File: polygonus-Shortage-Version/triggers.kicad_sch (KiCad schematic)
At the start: 29 parts, among them U10 SRV05-4, U1202 SN74LVC2G17DB, U1207 SN74LVC2G17DB, U1208 SN74LVC2G17DB, U7 SRV05-4

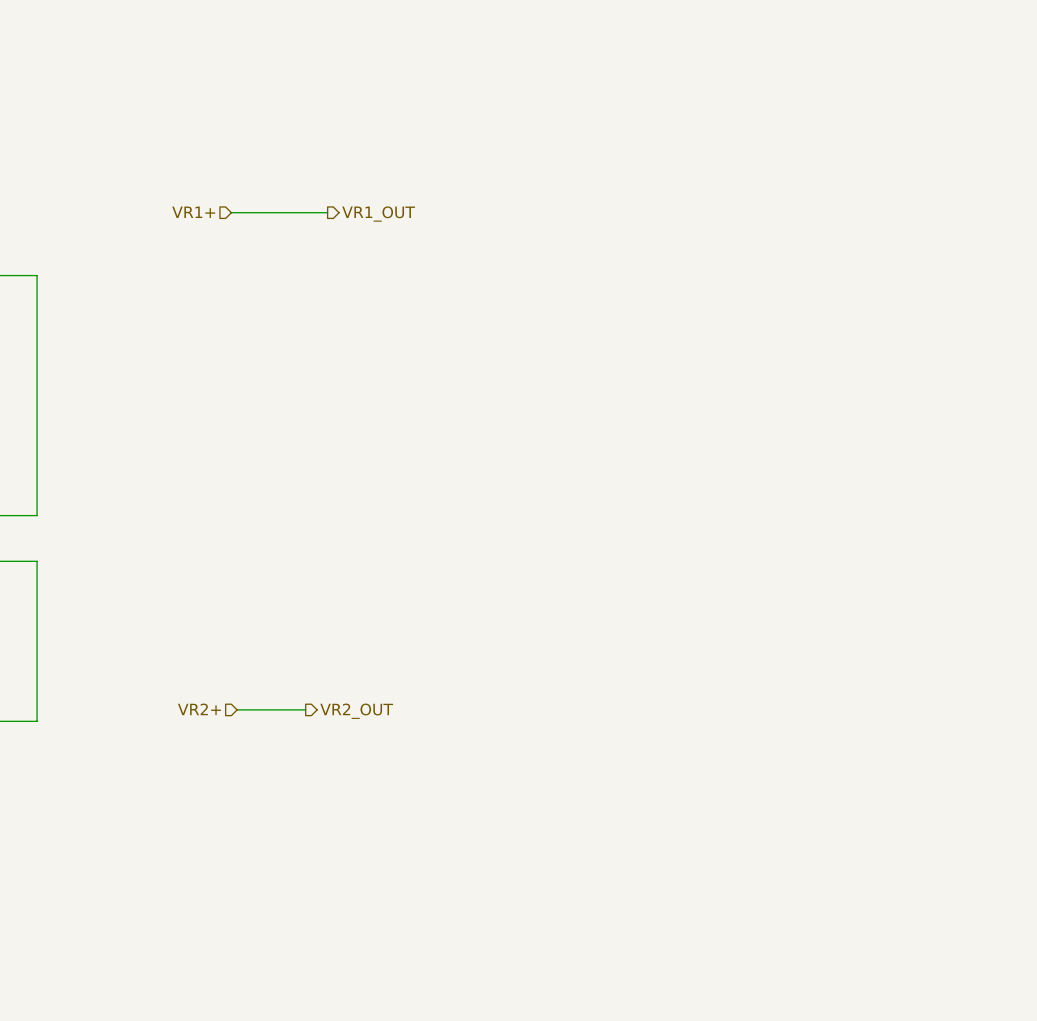
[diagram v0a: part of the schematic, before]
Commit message: Added Hall input stuff for VR pins
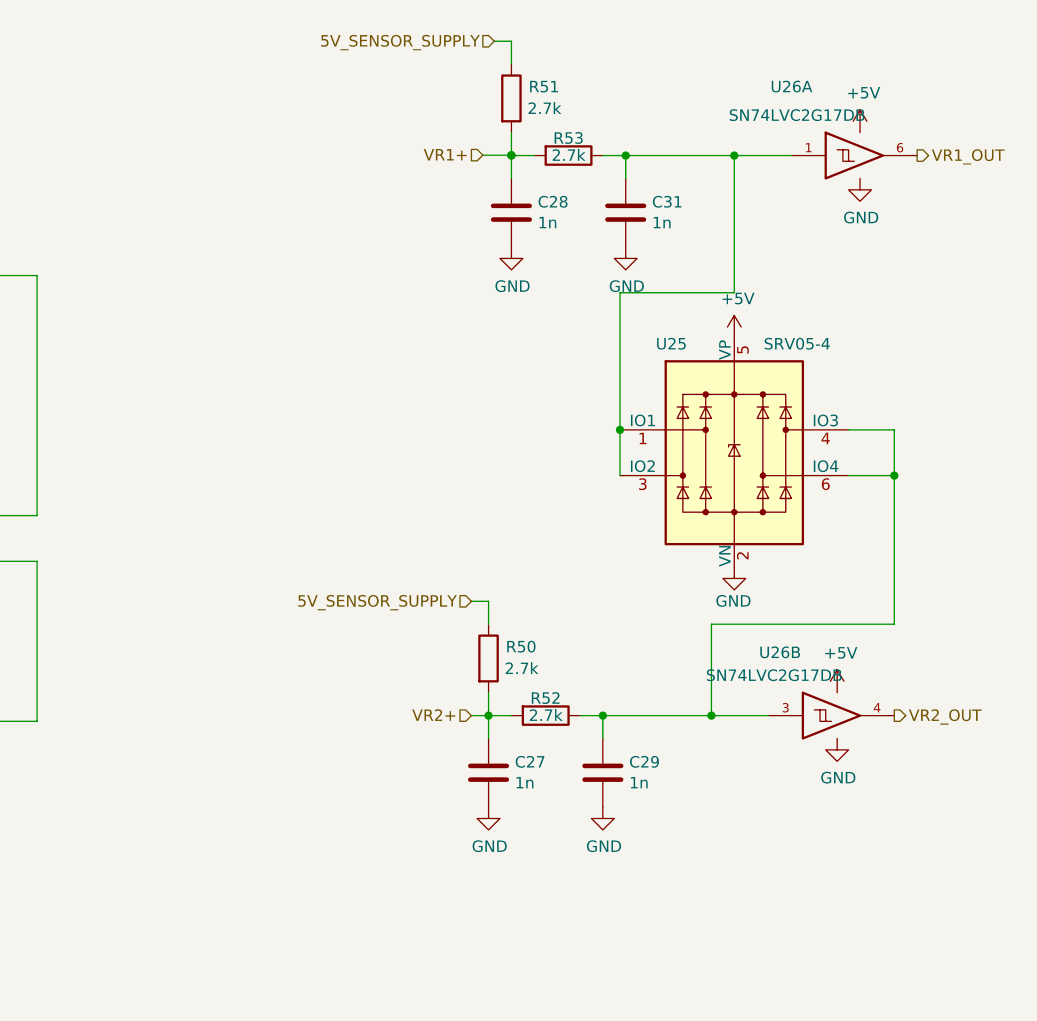
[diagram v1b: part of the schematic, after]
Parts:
- added C27, C28, C29, C31: 1n, Capacitor_SMD:C_0603_1608Metric, symbol Device:C
- added R50, R51, R52, R53: 2.7k, Resistor_SMD:R_0603_1608Metric, symbol Device:R
- added U25: SRV05-4, Package_TO_SOT_SMD:SOT-23-6, symbol Power_Protection:SRV05-4
- added U26: SN74LVC2G17DB, Package_TO_SOT_SMD:SOT-23-6, symbol 74xGxx:74LVC2G17
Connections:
- net +5V: now also U25.5 (VP), U26.5 (VCC), U26.5 (VCC)
- net 5V_SENSOR_SUPPLY: now also R50.1, R51.1
- net GND: now also C27.2, C28.2, C29.2, C31.2, U25.2 (VN), U26.2 (GND), U26.2 (GND)
- net VR1+: now also C28.1, R51.2, R53.2
- net VR2+: now also C27.1, R50.2, R52.2
- new net: C31.1, R53.1, U25.1 (IO1), U25.3 (IO2), U26.1
- new net: C29.1, R52.1, U25.4 (IO3), U25.6 (IO4), U26.3
- new net VR1_OUT: U26.6
- new net VR2_OUT: U26.4

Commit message: clearout basic version
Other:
- company: rusEFI -> (none)
- title: rusEfi Proteus -> Polygonus
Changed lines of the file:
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@@
   (paper "A4")
   (title_block
-    (title "rusEfi Proteus")
-    (date "2022-04-09")
+    (title "Polygonus")
+    (date "2023-03-15")
     (rev "v0.7")
-    (company "rusEFI")
-    (comment 1 "github.com/mck1117/proteus")
     (comment 2 "rusefi.com/s/proteus")
   )

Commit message: Update to V1.3
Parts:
- renumbered C1401 to C24, C1403 to C25, C1405 to C26, C1407 to C27, C1204 to C28, C1207 to C29, C1402 to C30, C1404 to C31, C1406 to C32, C1408 to C33, C1205 to C34, C1208 to C35, C27 to C36, C28 to C37, C29 to C38, C31 to C39, R1401 to R23, R1403 to R24, R1405 to R25, R1407 to R26, R1201 to R27, R1203 to R28, R1402 to R29, R1404 to R30, R1406 to R31, R1408 to R32, R1202 to R33, R1204 to R34, R50 to R35, R51 to R36, R52 to R37, R53 to R38, U1202 to U10, U7 to U11, U10 to U12, U25 to U13, U26 to U14, U1207 to U8, U1208 to U9
